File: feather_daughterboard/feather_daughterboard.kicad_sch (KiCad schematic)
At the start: 2 parts

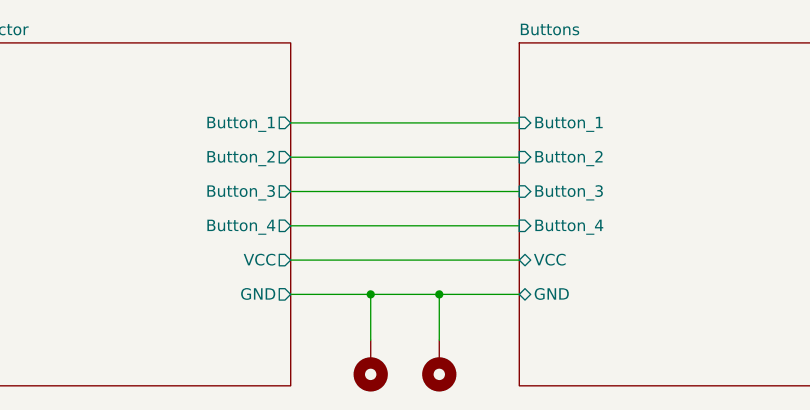
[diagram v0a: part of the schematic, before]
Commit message: changed the connector on the daughter board
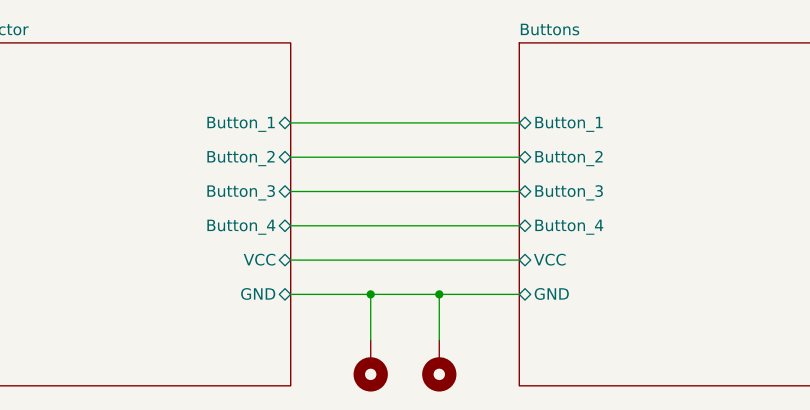
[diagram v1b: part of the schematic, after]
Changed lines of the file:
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@@
 			)
 		)
-		(pin "Button_2" input
+		(pin "Button_2" bidirectional
 			(at 165.1 88.9 180)
 			(effects
@@
 			)
 		)
-		(pin "Button_1" input
+		(pin "Button_1" bidirectional
 			(at 165.1 85.09 180)
 			(effects
@@
 			)
 		)
-		(pin "Button_4" input
+		(pin "Button_4" bidirectional
 			(at 165.1 96.52 180)
 			(effects
@@
 			)
 		)
-		(pin "Button_3" input
+		(pin "Button_3" bidirectional
 			(at 165.1 92.71 180)
 			(effects
@@
 			)
 		)
-		(pin "Button_1" output
+		(pin "Button_1" bidirectional
 			(at 139.7 85.09 0)
 			(effects
@@
 			)
 		)
-		(pin "VCC" output
+		(pin "VCC" bidirectional
 			(at 139.7 100.33 0)
 			(effects
@@
 			)
 		)
-		(pin "Button_2" output
+		(pin "Button_2" bidirectional
 			(at 139.7 88.9 0)
 			(effects
@@
 			)
 		)
-		(pin "Button_3" output
+		(pin "Button_3" bidirectional
 			(at 139.7 92.71 0)
 			(effects
@@
 			)
 		)
-		(pin "Button_4" output
+		(pin "Button_4" bidirectional
 			(at 139.7 96.52 0)
 			(effects
@@
 			)
 		)
-		(pin "GND" output
+		(pin "GND" bidirectional
 			(at 139.7 104.14 0)
 			(effects

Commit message: finished mainboard and daughterboard
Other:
- company: (none) -> bklaric
- title: (none) -> Feather Daughterboard
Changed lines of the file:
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@@
 	(generator_version "8.0")
 	(paper "A4")
+	(title_block
+		(title "Feather Daughterboard")
+		(date "2024-10-30")
+		(rev "1")
+		(company "bklaric")
+		(comment 4 "lprd_feather_daughterboard")
+	)
 	(junction
 		(at 148.59 104.14)

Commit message: added bigger logo and labeled the pins on the connectors
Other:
- company: bklaric -> Benjamin Klaric
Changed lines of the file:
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@@
 		(date "2024-10-30")
 		(rev "1")
-		(company "bklaric")
+		(company "Benjamin Klaric")
 		(comment 4 "lprd_feather_daughterboard")
 	)

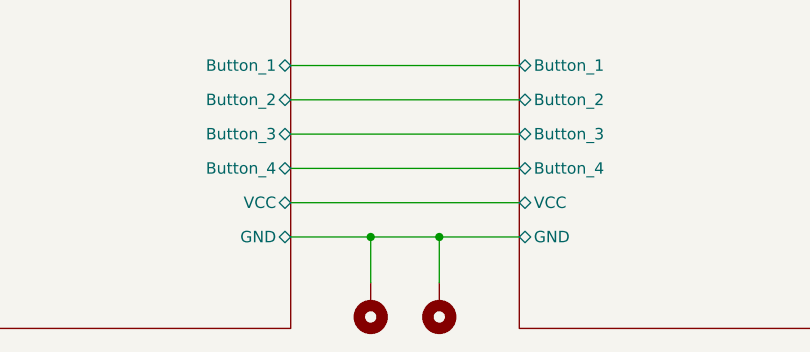
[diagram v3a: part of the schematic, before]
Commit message: Small changes to silkscreen text
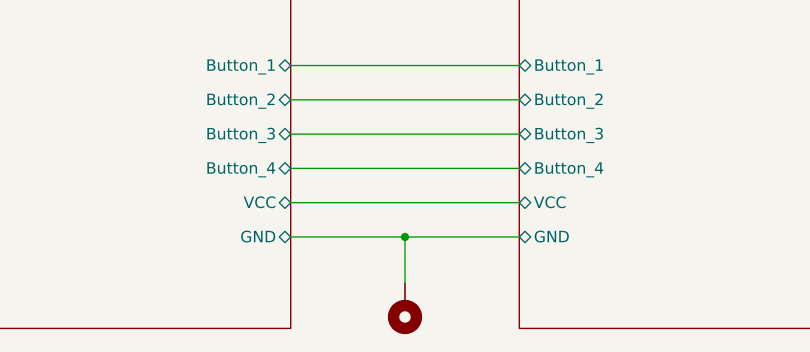
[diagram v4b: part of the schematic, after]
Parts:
- removed H1: MountingHole_Pad, MountingHole:MountingHole_2.2mm_M2_DIN965_Pad, symbol Mechanical:MountingHole_Pad
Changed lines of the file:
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@@
 	)
 	(junction
-		(at 148.59 104.14)
-		(diameter 0)
-		(color 0 0 0 0)
-	)
-	(junction
-		(at 156.21 104.14)
+		(at 152.4 104.14)
 		(diameter 0)
 		(color 0 0 0 0)
@@
 	(wire
 		(pts
-			(xy 148.59 104.14) (xy 156.21 104.14)
-		)
-		(stroke
-			(width 0)
-			(type default)
-		)
-	)
-	(wire
-		(pts
-			(xy 139.7 104.14) (xy 148.59 104.14)
+			(xy 139.7 104.14) (xy 152.4 104.14)
 		)
 		(stroke
@@
 	(wire
 		(pts
-			(xy 156.21 104.14) (xy 156.21 109.22)
+			(xy 152.4 104.14) (xy 152.4 109.22)
 		)
 		(stroke
@@
 	(wire
 		(pts
-			(xy 148.59 104.14) (xy 148.59 109.22)
-		)
-		(stroke
-			(width 0)
-			(type default)
-		)
-	)
-	(wire
-		(pts
 			(xy 139.7 85.09) (xy 165.1 85.09)
 		)
@@
 	(wire
 		(pts
-			(xy 156.21 104.14) (xy 165.1 104.14)
+			(xy 152.4 104.14) (xy 165.1 104.14)
 		)
 		(stroke
@@
 	(symbol
 		(lib_id "Mechanical:MountingHole_Pad")
-		(at 156.21 111.76 180)
+		(at 152.4 111.76 180)
 		(unit 1)
 		(exclude_from_sim yes)
@@
 		(fields_autoplaced yes)
 		(property "Reference" "H2"
-			(at 158.75 111.7599 0)
+			(at 154.94 111.7599 0)
 			(effects
 				(font
@@
 		)
 		(property "Value" "MountingHole_Pad"
-			(at 158.75 114.2999 0)
+			(at 154.94 114.2999 0)
 			(effects
 				(font
@@
 		)
 		(property "Footprint" "MountingHole:MountingHole_2.2mm_M2_DIN965_Pad"
-			(at 156.21 111.76 0)
+			(at 152.4 111.76 0)
 			(effects
 				(font
@@
 		)
 		(property "Datasheet" "~"
-			(at 156.21 111.76 0)
+			(at 152.4 111.76 0)
 			(effects
 				(font
@@
 		)
 		(property "Description" "Mounting Hole with connection"
-			(at 156.21 111.76 0)
+			(at 152.4 111.76 0)
 			(effects
 				(font
@@
 					(unit 1)
 				)
-			)
-		)
-	)
-	(symbol
-		(lib_id "Mechanical:MountingHole_Pad")
-		(at 148.59 111.76 180)
-		(unit 1)
-		(exclude_from_sim yes)
-		(in_bom no)
-		(on_board yes)
-		(dnp no)
-		(fields_autoplaced yes)
-		(property "Reference" "H1"
-			(at 151.13 111.7599 0)
-			(effects
-				(font
-					(size 1.27 1.27)
-				)
-				(justify right)
-				(hide yes)
-			)
-		)
-		(property "Value" "MountingHole_Pad"
-			(at 151.13 114.2999 0)
-			(effects
-				(font
-					(size 1.27 1.27)
-				)
-				(justify right)
-				(hide yes)
-			)
-		)
-		(property "Footprint" "MountingHole:MountingHole_2.2mm_M2_DIN965_Pad"
-			(at 148.59 111.76 0)
-			(effects
-				(font
-					(size 1.27 1.27)
-				)
-				(hide yes)
-			)
-		)
-		(property "Datasheet" "~"
-			(at 148.59 111.76 0)
-			(effects
-				(font
-					(size 1.27 1.27)
-				)
-				(hide yes)
-			)
-		)
-		(property "Description" "Mounting Hole with connection"
-			(at 148.59 111.76 0)
-			(effects
-				(font
-					(size 1.27 1.27)
-				)
-				(hide yes)
-			)
-		)
-		(pin "1"
-		)
-		(instances
-			(project "feather_daughterboard"
-				(path "/f87bd391-02e1-482b-840f-25c34f805c61"
-					(reference "H1")
-					(unit 1)
-				)

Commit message: Updated Daughterboard and added Gerber files
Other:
- sheet Buttons renamed Board
- note added: "R1_x -> 10 kΩ R3_x -> 75 kΩ C1_x -> 100 nF"
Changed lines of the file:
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@@
+		)
+	)
+	(text "R1_x -> 10 kΩ\nR3_x -> 75 kΩ\nC1_x -> 100 nF"
+		(exclude_from_sim no)
+		(at 245.872 158.75 0)
+		(effects
+			(font
+				(size 3 3)
+			)
+			(justify left)
 		)
 	)
@@
 		)
 		(fill
-			(color 248 237 193 1.0000)
-		)
-		(property "Sheetname" "Buttons"
+			(color 128 253 127 1.0000)
+		)
+		(property "Sheetname" "Board"
 			(at 165.1 75.4884 0)
 			(effects
@@
 				(font
 					(size 1.27 1.27)
+					(color 132 0 0 1)
 				)
 				(justify left)
@@
 				(font
 					(size 1.27 1.27)
+					(color 132 0 0 1)
 				)
 				(justify left)
@@
 				(font
 					(size 1.27 1.27)
+					(color 132 0 0 1)
 				)
 				(justify left)
@@
 				(font
 					(size 1.27 1.27)
+					(color 132 0 0 1)
 				)
 				(justify left)
@@
 				(font
 					(size 1.27 1.27)
+					(color 132 0 0 1)
 				)
 				(justify left)
@@
 				(font
 					(size 1.27 1.27)
+					(color 132 0 0 1)
 				)
 				(justify left)
@@
 		)
 		(fill
-			(color 248 237 193 1.0000)
+			(color 128 253 127 1.0000)
 		)
 		(property "Sheetname" "Connector"
@@
 				(font
 					(size 1.27 1.27)
+					(color 132 0 0 1)
 				)
 				(justify right)
@@
 				(font
 					(size 1.27 1.27)
+					(color 132 0 0 1)
 				)
 				(justify right)
@@
 				(font
 					(size 1.27 1.27)
+					(color 132 0 0 1)
 				)
 				(justify right)
@@
 				(font
 					(size 1.27 1.27)
+					(color 132 0 0 1)
 				)
 				(justify right)
@@
 				(font
 					(size 1.27 1.27)
+					(color 132 0 0 1)
 				)
 				(justify right)
@@
 				(font
 					(size 1.27 1.27)
-				)
-				(justify right)
+					(color 132 0 0 1)
+				)
+				(justify right)
